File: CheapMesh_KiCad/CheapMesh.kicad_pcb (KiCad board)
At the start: 2 copper layers, 34.8 x 67.3 mm, 24 parts, among them J1 Conn_01x02_Pin, J2 Conn_01x09_Pin, J3 USB_A, J4 USB_C, J5 Conn_Coaxial, Q1 UMH3N, U1 L78L33, U2 HT-CT62, U3 AP2112K-3.3

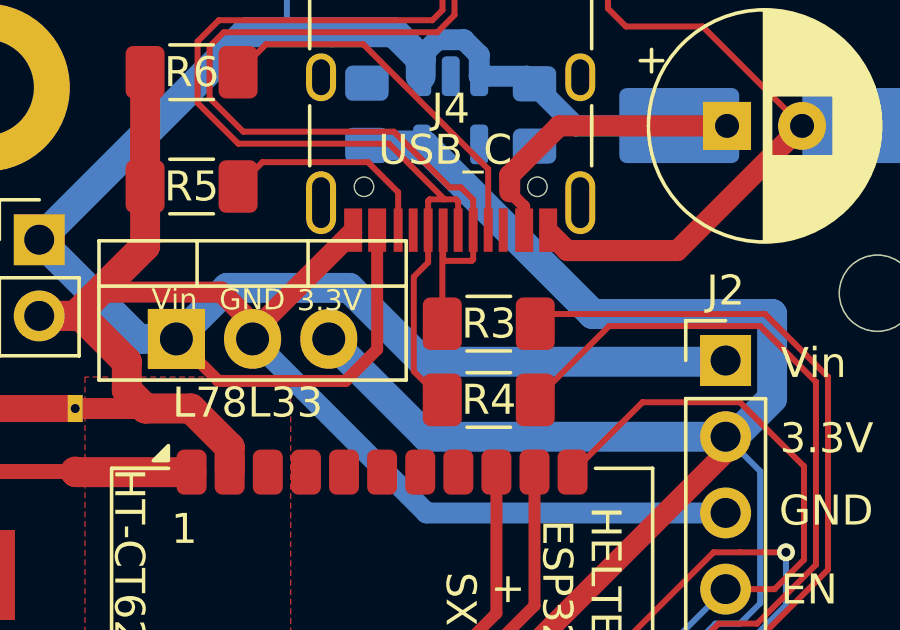
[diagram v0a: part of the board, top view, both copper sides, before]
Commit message: invert USB_D+ USB_D- in pcb
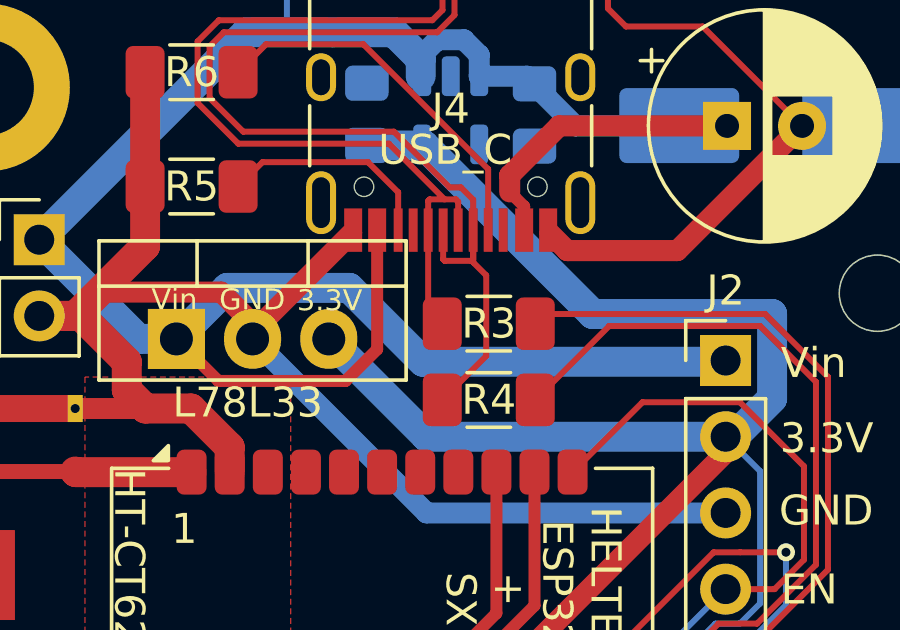
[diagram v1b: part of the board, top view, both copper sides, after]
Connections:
- R3 pad 1: Net-(J3-D-) -> Net-(J3-D+)
- R3 pad 2: USB_D- -> USB_D+
- R4 pad 1: Net-(J3-D+) -> Net-(J3-D-)
- R4 pad 2: USB_D+ -> USB_D-
- U2 pad 17: USB_D+ -> USB_D-
- U2 pad 18: USB_D- -> USB_D+
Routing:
- net Net-(J3-D-): track 34.0 -> 37.3 mm
- net Net-(J3-D+): track 38.6 -> 35.7 mm
- net USB_D-: track 38.1 -> 39.1 mm
- net USB_D+: track 39.1 -> 38.1 mm
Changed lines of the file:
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@@
 			(layers "F.Cu" "F.Paste" "F.Mask")
 			(roundrect_rratio 0.25)
-			(net 19 "USB_D+")
+			(net 20 "USB_D-")
 			(pinfunction "GPIO18_DN")
 			(pintype "bidirectional")
@@
 			(layers "F.Cu" "F.Paste" "F.Mask")
 			(roundrect_rratio 0.25)
-			(net 20 "USB_D-")
+			(net 19 "USB_D+")
 			(pinfunction "GPIO19_DP")
 			(pintype "bidirectional")
@@
 			(layers "F.Cu" "F.Paste" "F.Mask")
 			(roundrect_rratio 0.1923076923)
-			(net 26 "Net-(J3-D-)")
+			(net 27 "Net-(J3-D+)")
 			(pintype "passive")
 		)
@@
 			(layers "F.Cu" "F.Paste" "F.Mask")
 			(roundrect_rratio 0.1923076923)
-			(net 20 "USB_D-")
+			(net 19 "USB_D+")
 			(pintype "passive")
 		)
@@
 			(layers "F.Cu" "F.Paste" "F.Mask")
 			(roundrect_rratio 0.1923076923)
-			(net 27 "Net-(J3-D+)")
+			(net 26 "Net-(J3-D-)")
 			(pintype "passive")
 		)
@@
 			(layers "F.Cu" "F.Paste" "F.Mask")
 			(roundrect_rratio 0.1923076923)
-			(net 19 "USB_D+")
+			(net 20 "USB_D-")
 			(pintype "passive")
 		)
@@
 	)
 	(segment
-		(start 59.69 142.623654)
-		(end 59.69 144.094314)
+		(start 62.13 143.436346)
+		(end 61.216346 144.35)
 		(width 0.2)
 		(layer "F.Cu")
@@
 	)
 	(segment
-		(start 62.13 131.65)
-		(end 63.992 133.512)
+		(start 61.216346 144.35)
+		(end 60 144.35)
 		(width 0.2)
 		(layer "F.Cu")
@@
 	)
 	(segment
-		(start 62.028215 141.57)
-		(end 60.743654 141.57)
+		(start 62.13 142.033901)
+		(end 62.13 143.436346)
 		(width 0.2)
 		(layer "F.Cu")
@@
 	)
 	(segment
-		(start 63.992 133.512)
-		(end 63.992 139.606215)
+		(start 50.8 153.55)
+		(end 50.8 154.3)
 		(width 0.2)
 		(layer "F.Cu")
@@
 	)
 	(segment
-		(start 49.53 154.3)
-		(end 49.764 154.534)
-		(width 0.4)
+		(start 60 144.35)
+		(end 50.8 153.55)
+		(width 0.2)
 		(layer "F.Cu")
 		(net 19)
 	)
 	(segment
-		(start 57.098 131.65)
-		(end 62.13 131.65)
+		(start 54.636 131.572)
+		(end 54.958 131.25)
 		(width 0.2)
 		(layer "F.Cu")
@@
 	)
 	(segment
-		(start 63.992 139.606215)
-		(end 62.028215 141.57)
+		(start 64.392 139.771901)
+		(end 62.13 142.033901)
 		(width 0.2)
 		(layer "F.Cu")
@@
 	)
 	(segment
-		(start 50.315256 153.25)
-		(end 49.53 154.035256)
+		(start 54.958 131.25)
+		(end 62.295686 131.25)
 		(width 0.2)
 		(layer "F.Cu")
@@
 	)
 	(segment
-		(start 59.69 144.094314)
-		(end 50.534314 153.25)
+		(start 62.295686 131.25)
+		(end 64.392 133.346315)
 		(width 0.2)
 		(layer "F.Cu")
@@
 	)
 	(segment
-		(start 49.53 154.035256)
-		(end 49.53 154.3)
+		(start 64.392 133.346315)
+		(end 64.392 139.771901)
 		(width 0.2)
 		(layer "F.Cu")
@@
 	)
 	(segment
-		(start 50.534314 153.25)
-		(end 50.315256 153.25)
+		(start 59.69 142.623654)
+		(end 59.69 144.094314)
 		(width 0.2)
 		(layer "F.Cu")
-		(net 19)
+		(net 20)
 	)
 	(segment
-		(start 60.743654 141.57)
-		(end 59.69 142.623654)
+		(start 62.13 131.65)
+		(end 63.992 133.512)
 		(width 0.2)
 		(layer "F.Cu")
-		(net 19)
+		(net 20)
 	)
 	(segment
-		(start 54.636 134.112)
-		(end 57.098 131.65)
+		(start 62.028215 141.57)
+		(end 60.743654 141.57)
 		(width 0.2)
 		(layer "F.Cu")
-		(net 19)
+		(net 20)
 	)
 	(segment
-		(start 62.13 143.436346)
-		(end 61.216346 144.35)
+		(start 63.992 133.512)
+		(end 63.992 139.606215)
 		(width 0.2)
 		(layer "F.Cu")
@@
 	)
 	(segment
-		(start 61.216346 144.35)
-		(end 60 144.35)
-		(width 0.2)
+		(start 49.53 154.3)
+		(end 49.764 154.534)
+		(width 0.4)
 		(layer "F.Cu")
 		(net 20)
 	)
 	(segment
-		(start 62.13 142.033901)
-		(end 62.13 143.436346)
+		(start 57.098 131.65)
+		(end 62.13 131.65)
 		(width 0.2)
 		(layer "F.Cu")
@@
 	)
 	(segment
-		(start 50.8 153.55)
-		(end 50.8 154.3)
+		(start 63.992 139.606215)
+		(end 62.028215 141.57)
 		(width 0.2)
 		(layer "F.Cu")
@@
 	)
 	(segment
-		(start 60 144.35)
-		(end 50.8 153.55)
+		(start 50.315256 153.25)
+		(end 49.53 154.035256)
 		(width 0.2)
 		(layer "F.Cu")
@@
 	)
 	(segment
-		(start 54.636 131.572)
-		(end 54.958 131.25)
+		(start 59.69 144.094314)
+		(end 50.534314 153.25)
 		(width 0.2)
 		(layer "F.Cu")
@@
 	)
 	(segment
-		(start 64.392 139.771901)
-		(end 62.13 142.033901)
+		(start 49.53 154.035256)
+		(end 49.53 154.3)
 		(width 0.2)
 		(layer "F.Cu")
@@
 	)
 	(segment
-		(start 54.958 131.25)
-		(end 62.295686 131.25)
+		(start 50.534314 153.25)
+		(end 50.315256 153.25)
 		(width 0.2)
 		(layer "F.Cu")
@@
 	)
 	(segment
-		(start 62.295686 131.25)
-		(end 64.392 133.346315)
+		(start 60.743654 141.57)
+		(end 59.69 142.623654)
 		(width 0.2)
 		(layer "F.Cu")
@@
 	)
 	(segment
-		(start 64.392 133.346315)
-		(end 64.392 139.771901)
+		(start 54.636 134.112)
+		(end 57.098 131.65)
 		(width 0.2)
 		(layer "F.Cu")
@@
 	)
 	(segment
+		(start 51.536 134.112)
+		(end 53 132.648)
+		(width 0.2)
+		(layer "F.Cu")
+		(net 26)
+	)
+	(segment
 		(start 51.943 117.729)
 		(end 51.943 121.285)
@@
 	)
 	(segment
+		(start 53 132.648)
+		(end 53 129.962)
+		(width 0.2)
+		(layer "F.Cu")
+		(net 26)
+	)
+	(segment
 		(start 44.901456 125.1712)
 		(end 49.921686 125.1712)
@@
 	)
 	(segment
-		(start 51.536 131.572)
-		(end 51.536 128.483)
+		(start 51.536 128.483)
+		(end 51.566 128.453)
+		(width 0.2)
+		(layer "F.Cu")
+		(net 26)
+	)
+	(segment
+		(start 52.566 129.528)
+		(end 52.566 128.453)
 		(width 0.2)
 		(layer "F.Cu")
@@
 	)
 	(segment
-		(start 51.943 121.285)
-		(end 51.37 121.858)
+		(start 53 129.962)
+		(end 52.566 129.528)
 		(width 0.2)
 		(layer "F.Cu")
@@
 	)
 	(segment
-		(start 51.536 128.483)
-		(end 51.566 128.453)
+		(start 51.943 121.285)
+		(end 51.37 121.858)
 		(width 0.2)
 		(layer "F.Cu")
@@
 	)
 	(segment
-		(start 51.536 134.112)
-		(end 50.586 133.162)
-		(width 0.2)
-		(layer "F.Cu")
-		(net 27)
-	)
-	(segment
 		(start 52.066 127.504)
 		(end 52.066 128.453)
@@
 	)
 	(segment
-		(start 51.116 127.428)
-		(end 51.99 127.428)
+		(start 51.536 131.572)
+		(end 51.066 131.102)
 		(width 0.2)
 		(layer "F.Cu")
@@
 	)
 	(segment
-		(start 50.586 130.008)
-		(end 51.066 129.528)
+		(start 51.116 127.428)
+		(end 51.99 127.428)
 		(width 0.2)
 		(layer "F.Cu")
@@
 	)
 	(segment
-		(start 51.066 129.528)
+		(start 51.066 131.102)
 		(end 51.066 128.453)
 		(width 0.2)
 		(layer "F.Cu")
-		(net 27)
-	)
-	(segment
-		(start 50.586 133.162)
-		(end 50.586 130.008)
-		(width 0.2)
-		(layer "F.Cu")

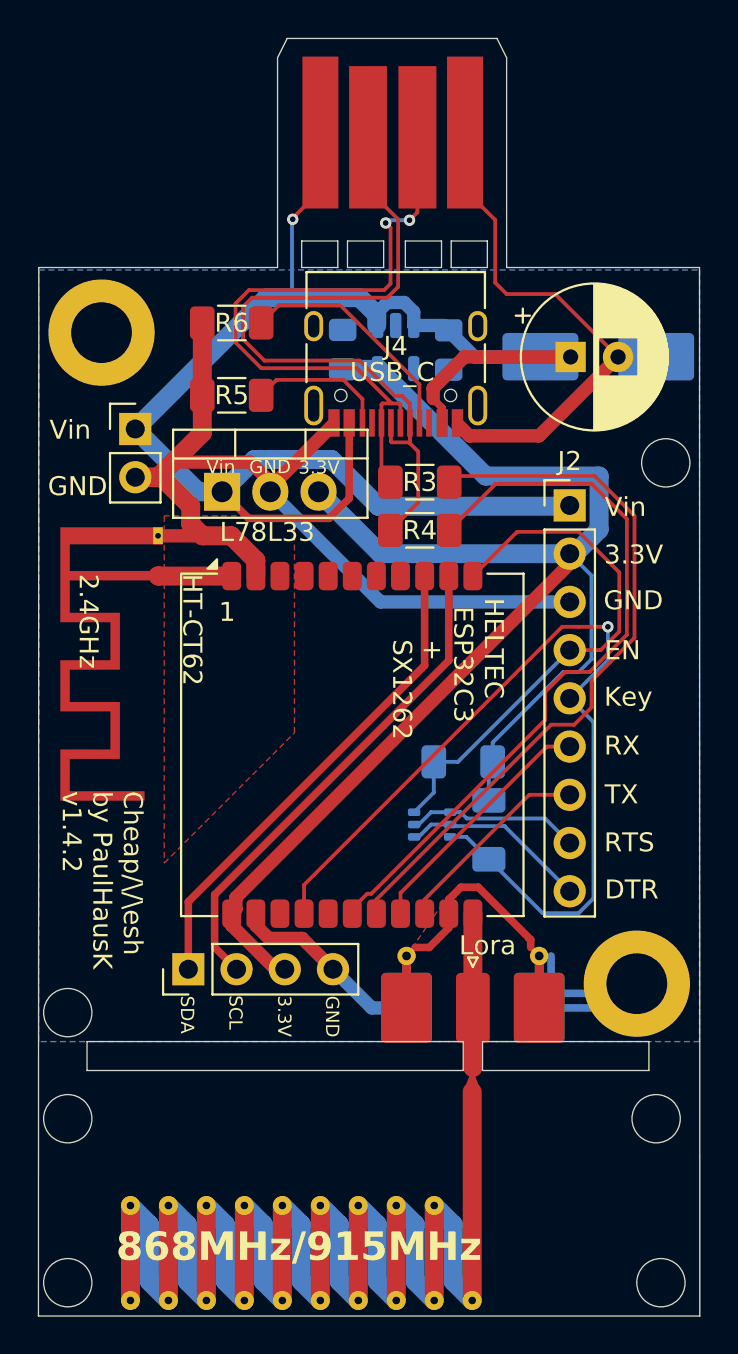
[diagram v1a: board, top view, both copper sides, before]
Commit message: add gpio2 pin
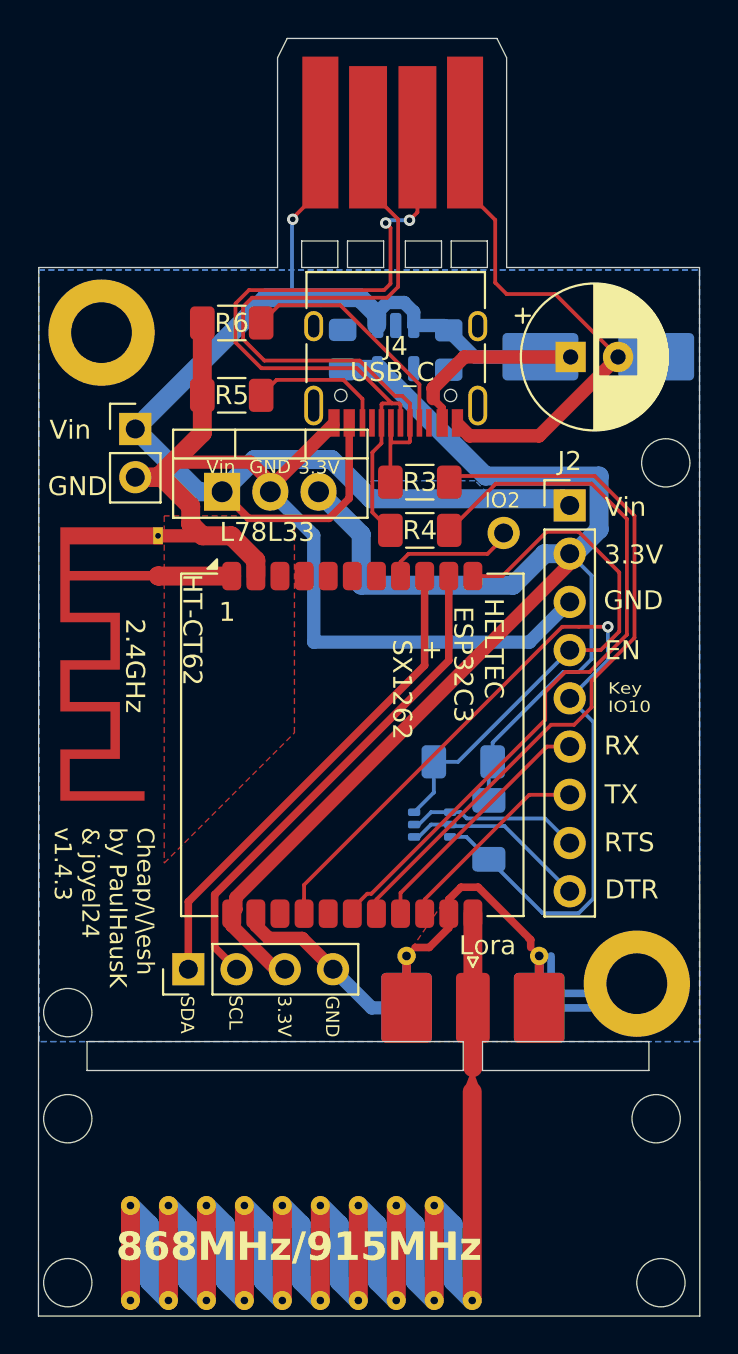
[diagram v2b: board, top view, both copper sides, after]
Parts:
- added ?: , , F.Cu at (57.5, 134.2)
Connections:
- R3 pad 1: Net-(J3-D+) -> Net-(J3-D-)
- R3 pad 2: USB_D+ -> USB_D-
- R4 pad 1: Net-(J3-D-) -> Net-(J3-D+)
- R4 pad 2: USB_D- -> USB_D+
- U2 pad 17: USB_D- -> USB_D+
- U2 pad 18: USB_D+ -> USB_D-
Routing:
- net unconnected-(U2-GPIO2-Pad8): track 0.00 -> 6.71 mm
- net GND: track 127.1 -> 132.2 mm
- net Net-(J3-D-): track 37.3 -> 34.0 mm
- net 3.3V: track 83.2 -> 86.1 mm
- net Net-(J3-D+): track 35.7 -> 38.6 mm
- net USB_D-: track 39.1 -> 38.1 mm
- net USB_D+: track 38.1 -> 39.1 mm
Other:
- board text added: "Cheap/\/\esh by PaulHausK & joyel24 v1.4.3"
- board text added: "IO2"
- board text added: "Key IO10"
- board text removed: "Cheap/\/\esh by PaulHausK v1.4.2"
- board text removed: "Key"

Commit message: fix HT-CT62 footprint
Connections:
- U2 pad 17: USB_D+ -> USB_D-
- U2 pad 18: USB_D- -> USB_D+
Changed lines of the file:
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@@
 			(layers "F.Cu" "F.Paste" "F.Mask")
 			(roundrect_rratio 0.25)
-			(net 19 "USB_D+")
+			(net 20 "USB_D-")
 			(pinfunction "GPIO18_DN")
 			(pintype "bidirectional")
@@
 			(layers "F.Cu" "F.Paste" "F.Mask")
 			(roundrect_rratio 0.25)
-			(net 20 "USB_D-")
+			(net 19 "USB_D+")
 			(pinfunction "GPIO19_DP")
 			(pintype "bidirectional")

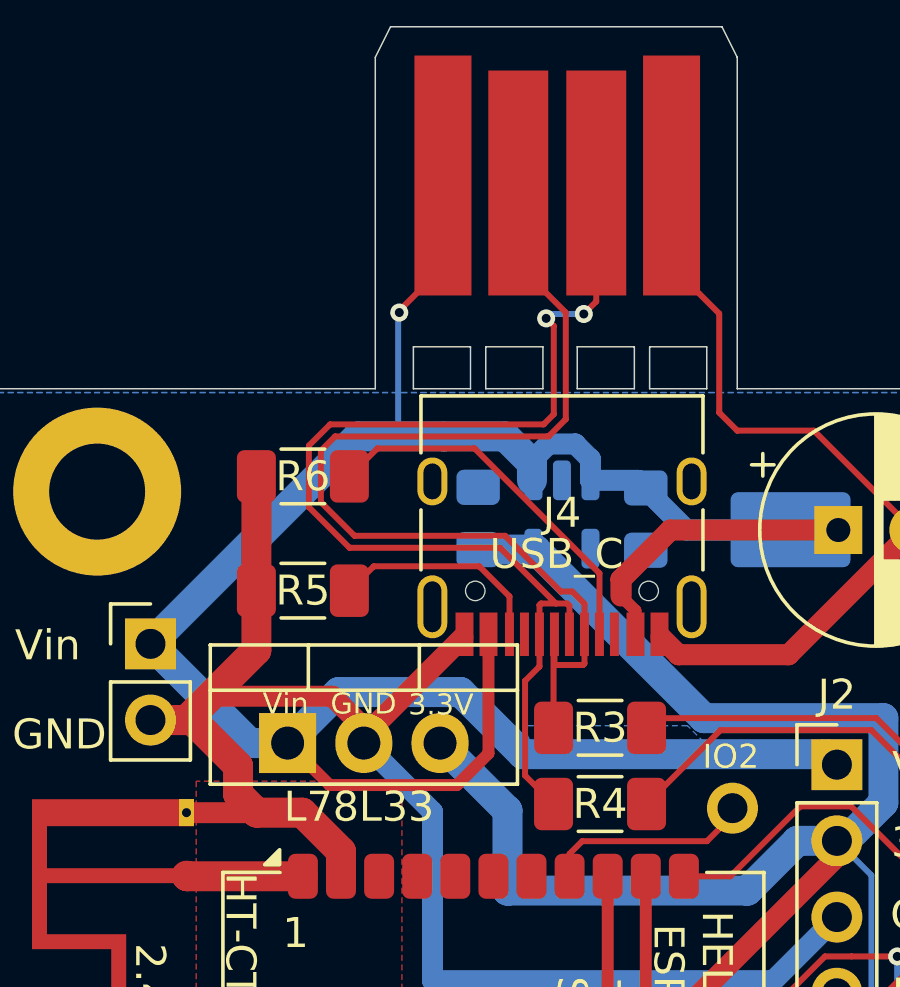
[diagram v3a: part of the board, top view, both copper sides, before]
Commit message: fix D+/- circuit
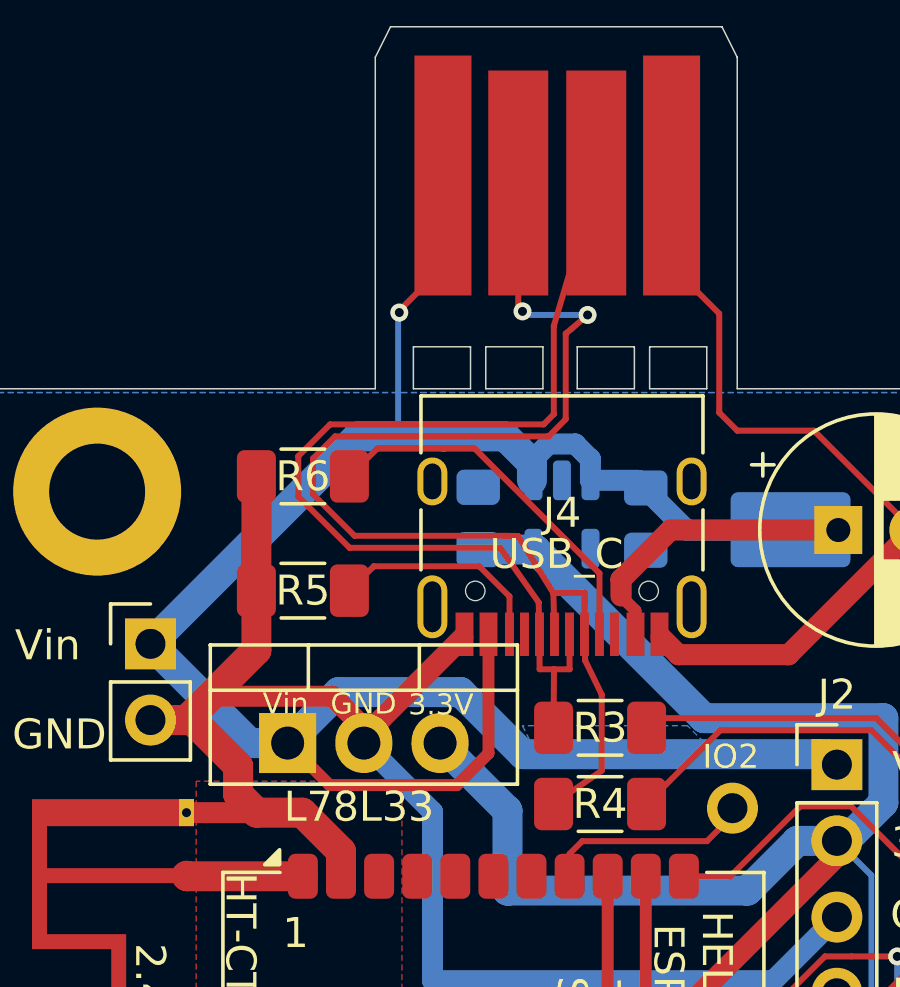
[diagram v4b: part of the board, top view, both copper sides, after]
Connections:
- R3 pad 1: Net-(J3-D-) -> Net-(J3-D+)
- R3 pad 2: USB_D- -> USB_D+
- R4 pad 1: Net-(J3-D+) -> Net-(J3-D-)
- R4 pad 2: USB_D+ -> USB_D-
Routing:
- net Net-(J3-D-): track 34.0 -> 42.7 mm, vias 0 -> 2
- net Net-(J3-D+): track 38.6 -> 34.4 mm, vias 2 -> 0
- net USB_D-: track 38.1 -> 39.1 mm
- net USB_D+: track 39.1 -> 38.1 mm
